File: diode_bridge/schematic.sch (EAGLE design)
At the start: 4 parts

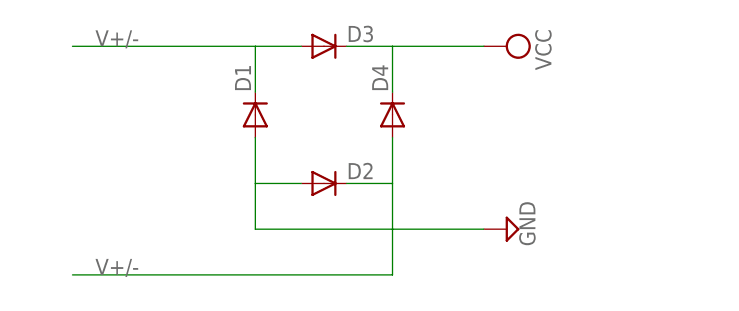
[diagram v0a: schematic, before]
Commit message: update diode bridge and readme
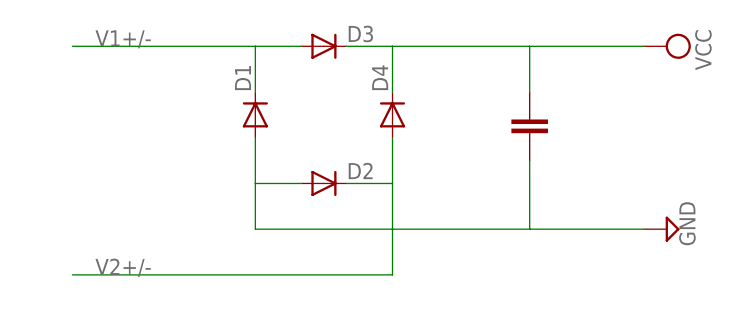
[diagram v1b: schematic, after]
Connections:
- removed net V+/-: D1.C, D2.C, D3.A, D4.A
- new net V1+/-: D1.C, D3.A
- new net V2+/-: D2.C, D4.A
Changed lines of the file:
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@@
 <part name="SUPPLY3" library="supply2" deviceset="GND" device=""/>
 <part name="SUPPLY4" library="supply2" deviceset="VCC" device=""/>
+<part name="C1" library="docu-dummy" deviceset="C" device=""/>
 </parts>
 <sheets>
@@
 <instance part="D3" gate="1" x="33.02" y="68.58"/>
 <instance part="D4" gate="1" x="40.64" y="60.96" rot="R90"/>
-<instance part="SUPPLY3" gate="GND" x="53.34" y="48.26" rot="R90"/>
-<instance part="SUPPLY4" gate="G$1" x="53.34" y="68.58" rot="R270"/>
+<instance part="SUPPLY3" gate="GND" x="71.12" y="48.26" rot="R90"/>
+<instance part="SUPPLY4" gate="G$1" x="71.12" y="68.58" rot="R270"/>
+<instance part="C1" gate="G$1" x="55.88" y="60.96"/>
 </instances>
 <busses>
 </busses>
 <nets>
-<net name="V+/-" class="0">
-<segment>
-<pinref part="D1" gate="1" pin="C"/>
-<wire x1="25.4" y1="63.5" x2="25.4" y2="68.58" width="0.1524" layer="91"/>
-<pinref part="D3" gate="1" pin="A"/>
-<wire x1="25.4" y1="68.58" x2="30.48" y2="68.58" width="0.1524" layer="91"/>
-<wire x1="25.4" y1="68.58" x2="5.08" y2="68.58" width="0.1524" layer="91"/>
-<label x="7.62" y="68.58" size="1.778" layer="95"/>
-</segment>
+<net name="V2+/-" class="0">
 <segment>
 <pinref part="D4" gate="1" pin="A"/>
@@
 <pinref part="D1" gate="1" pin="A"/>
 <wire x1="25.4" y1="53.34" x2="25.4" y2="58.42" width="0.1524" layer="91"/>
-<wire x1="50.8" y1="48.26" x2="25.4" y2="48.26" width="0.1524" layer="91"/>
+<wire x1="68.58" y1="48.26" x2="55.88" y2="48.26" width="0.1524" layer="91"/>
+<wire x1="55.88" y1="48.26" x2="25.4" y2="48.26" width="0.1524" layer="91"/>
 <wire x1="25.4" y1="48.26" x2="25.4" y2="53.34" width="0.1524" layer="91"/>
 <pinref part="SUPPLY3" gate="GND" pin="GND"/>
+<wire x1="55.88" y1="55.88" x2="55.88" y2="48.26" width="0.1524" layer="91"/>
 </segment>
 </net>
@@
 <wire x1="35.56" y1="68.58" x2="40.64" y2="68.58" width="0.1524" layer="91"/>
 <wire x1="40.64" y1="68.58" x2="40.64" y2="63.5" width="0.1524" layer="91"/>
-<wire x1="40.64" y1="68.58" x2="50.8" y2="68.58" width="0.1524" layer="91"/>
+<wire x1="40.64" y1="68.58" x2="55.88" y2="68.58" width="0.1524" layer="91"/>
 <pinref part="SUPPLY4" gate="G$1" pin="VCC"/>
+<wire x1="55.88" y1="68.58" x2="68.58" y2="68.58" width="0.1524" layer="91"/>
+<wire x1="55.88" y1="68.58" x2="55.88" y2="63.5" width="0.1524" layer="91"/>
 </segment>
 </net>
+<net name="V1+/-" class="0">
+<segment>
+<pinref part="D1" gate="1" pin="C"/>
+<wire x1="25.4" y1="63.5" x2="25.4" y2="68.58" width="0.1524" layer="91"/>
+<pinref part="D3" gate="1" pin="A"/>
+<wire x1="25.4" y1="68.58" x2="30.48" y2="68.58" width="0.1524" layer="91"/>
+<wire x1="25.4" y1="68.58" x2="5.08" y2="68.58" width="0.1524" layer="91"/>
+<label x="7.62" y="68.58" size="1.778" layer="95"/>
+</segment>
+</net>

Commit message: update schematics and remove .epf files
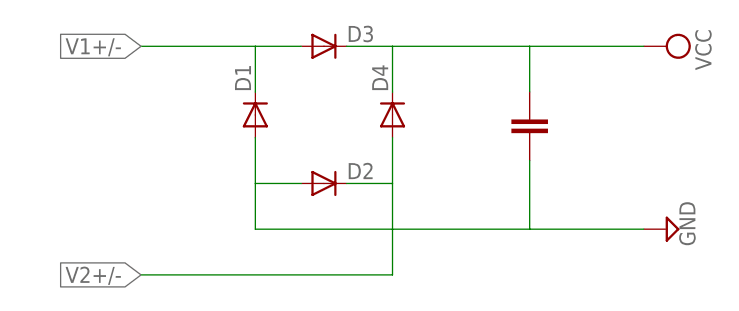
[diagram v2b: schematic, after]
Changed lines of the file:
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@@
 <wire x1="40.64" y1="53.34" x2="35.56" y2="53.34" width="0.1524" layer="91"/>
 <wire x1="40.64" y1="53.34" x2="40.64" y2="43.18" width="0.1524" layer="91"/>
-<wire x1="40.64" y1="43.18" x2="5.08" y2="43.18" width="0.1524" layer="91"/>
-<label x="7.62" y="43.18" size="1.778" layer="95"/>
+<wire x1="40.64" y1="43.18" x2="12.7" y2="43.18" width="0.1524" layer="91"/>
+<label x="12.7" y="43.18" size="1.778" layer="95" rot="MR0" xref="yes"/>
 </segment>
 </net>
@@
 <pinref part="D3" gate="1" pin="A"/>
 <wire x1="25.4" y1="68.58" x2="30.48" y2="68.58" width="0.1524" layer="91"/>
-<wire x1="25.4" y1="68.58" x2="5.08" y2="68.58" width="0.1524" layer="91"/>
-<label x="7.62" y="68.58" size="1.778" layer="95"/>
+<wire x1="25.4" y1="68.58" x2="12.7" y2="68.58" width="0.1524" layer="91"/>
+<label x="12.7" y="68.58" size="1.778" layer="95" rot="MR0" xref="yes"/>
 </segment>
 </net>
